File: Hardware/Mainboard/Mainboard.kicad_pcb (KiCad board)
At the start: 4 copper layers, 185.4 x 132.1 mm, 24 parts, among them IC1 TUSB2046BIRHBR, IC2 TUSB2046BIRHBR, IC3 TUSB2046BIRHBR, J1 Conn_02x10_Odd_Even, J10 Conn_02x04_Odd_Even, J11 Conn_02x04_Odd_Even, J12 ARJM11D7-009-AB-EW2, J13 USB4105-GF-A-060, J14 Conn_02x03_Odd_Even, J15 Conn_02x03_Odd_Even, J2 Conn_02x10_Odd_Even, J3 Conn_02x10_Odd_Even, J4 Conn_02x10_Odd_Even, J5 Conn_02x10_Odd_Even, J6 Conn_02x10_Odd_Even, J7 Conn_02x10_Odd_Even, J8 Conn_02x08_Odd_Even, J9 Conn_02x12_Odd_Even, P1 USB-A1HSW6, P2 USB-A1HSW6, SW1 SW_Push_Dual, SW2 SW_Push_Dual, U1 ENC624J600-I/PT, U2 SC0915

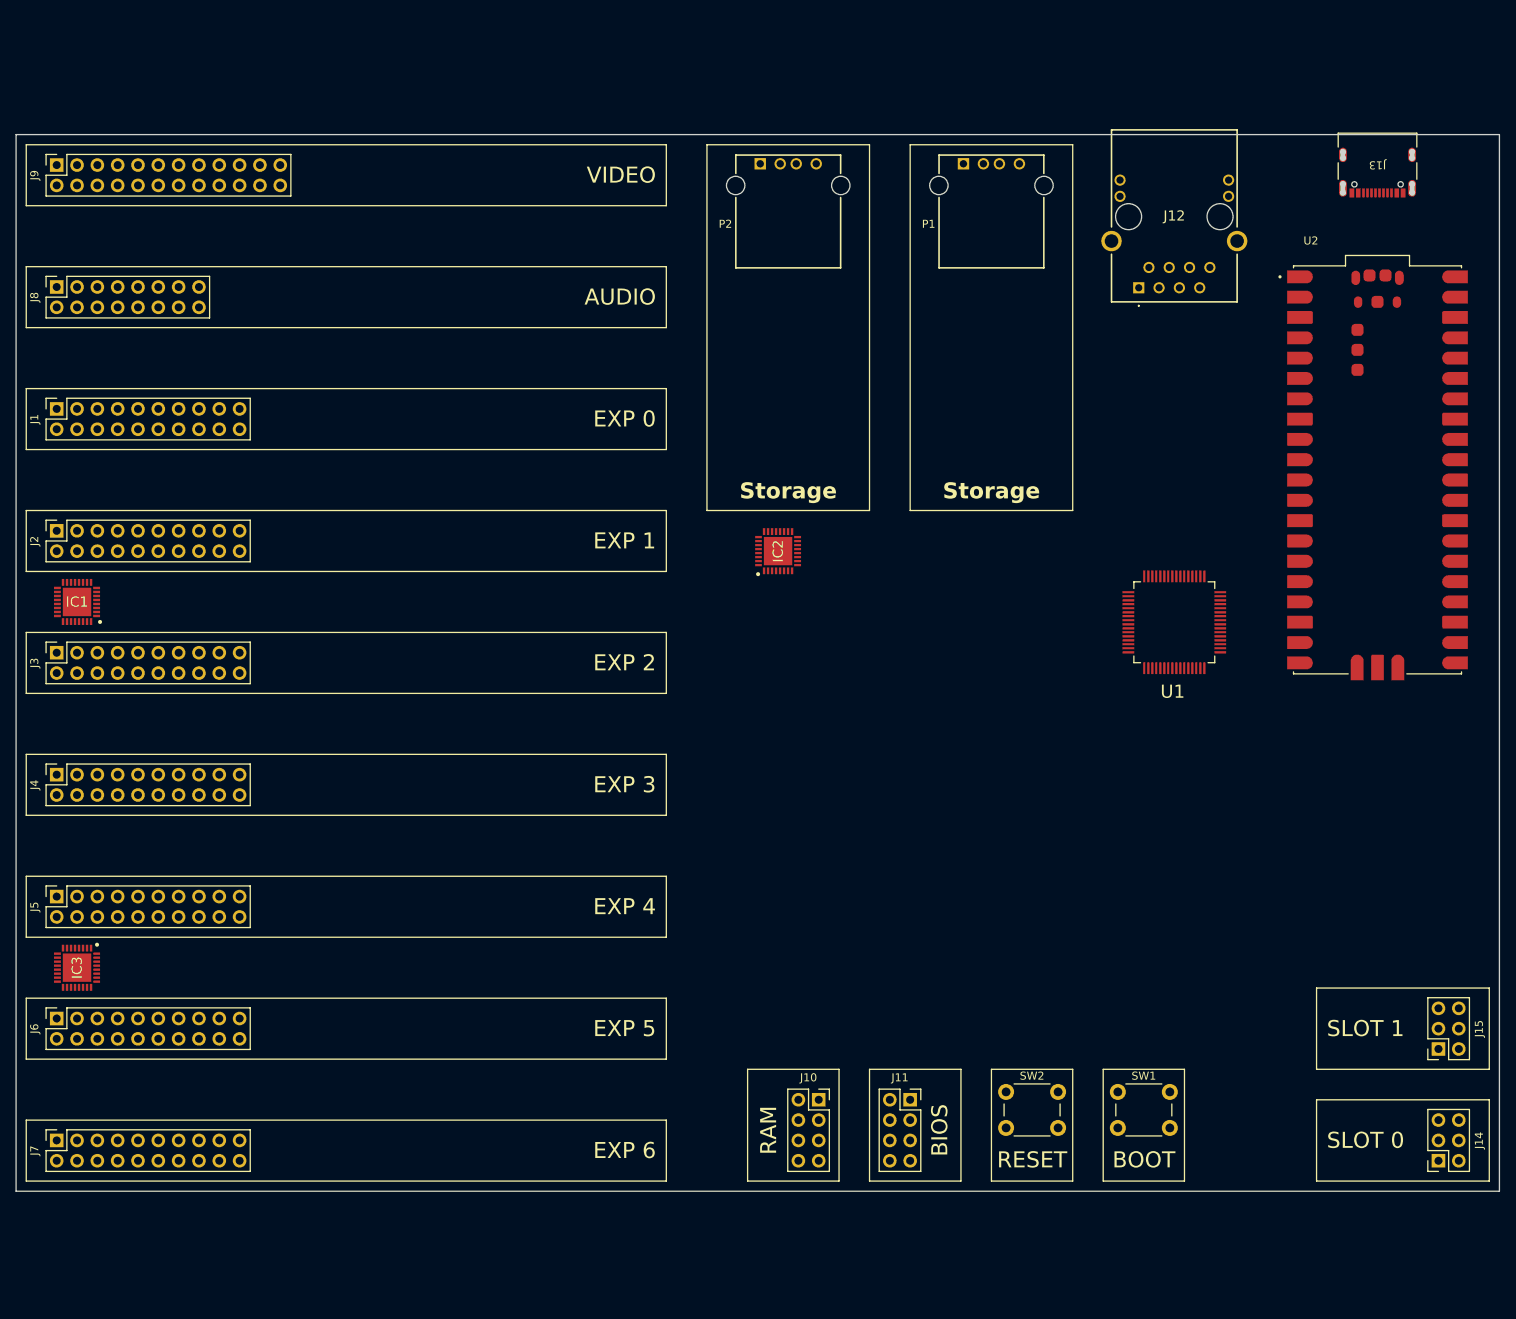
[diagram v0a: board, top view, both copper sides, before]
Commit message: Adds more work on the mainboard schematic
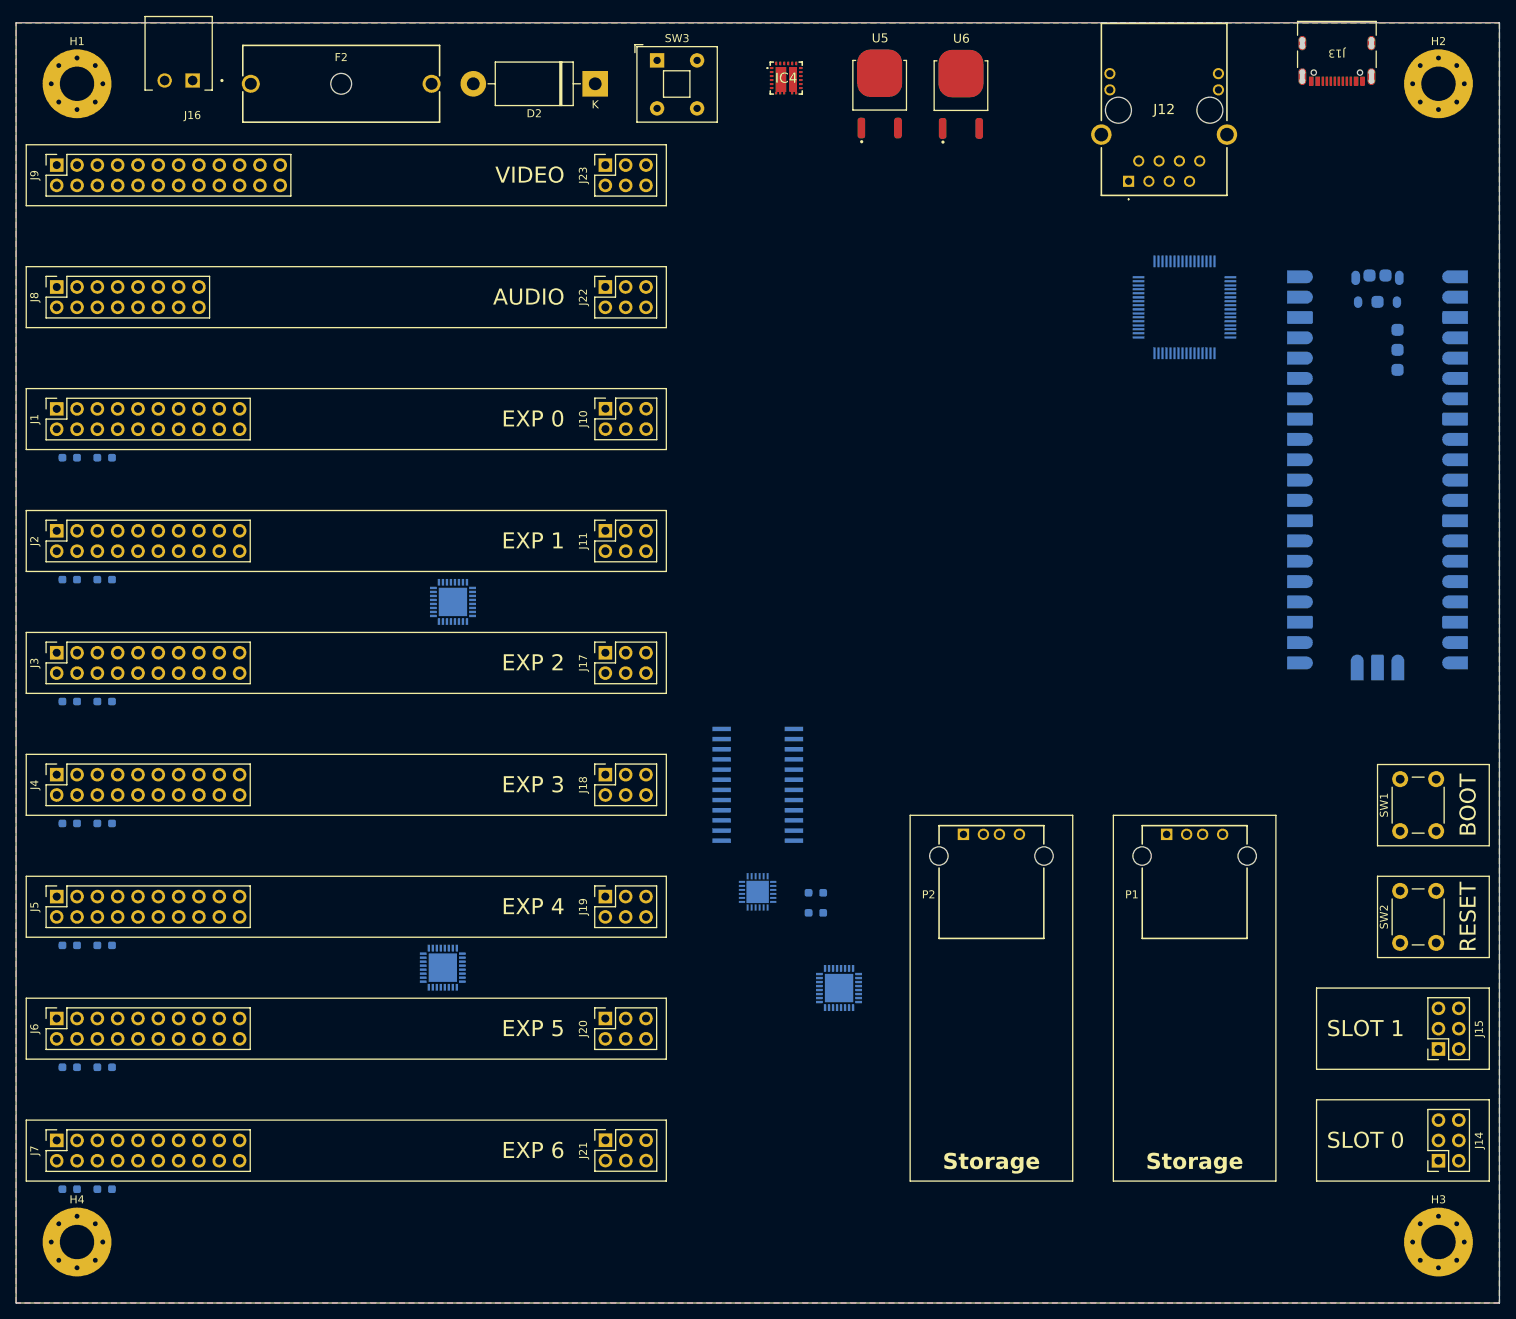
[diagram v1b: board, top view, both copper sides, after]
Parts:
- added D2: 1N5822, Diode_THT:D_DO-201AD_P15.24mm_Horizontal, F.Cu at (115.6, 40.6)
- added F2: 696107003002, compi:696107003002, F.Cu at (83.8, 40.6)
- added H1: MountingHole, MountingHole:MountingHole_4.3mm_M4_Pad_Via, F.Cu at (50.8, 40.6)
- added H2: MountingHole, MountingHole:MountingHole_4.3mm_M4_Pad_Via, F.Cu at (221.0, 40.6)
- added H3: MountingHole, MountingHole:MountingHole_4.3mm_M4_Pad_Via, F.Cu at (221.0, 185.4)
- added H4: MountingHole, MountingHole:MountingHole_4.3mm_M4_Pad_Via, F.Cu at (50.8, 185.4)
- added IC4: AOZ2261NQI-11, compi:aoz2261ngl-11, F.Cu at (139.4, 39.9)
- added J16: 1844210, compi:combicon-1844210, F.Cu at (63.5, 36.8)
- added J17: Conn_02x03_Counter_Clockwise, Connector_PinSocket_2.54mm:PinSocket_2x03_P2.54mm_Vertical, F.Cu at (116.8, 111.8)
- added J18: Conn_02x03_Counter_Clockwise, Connector_PinSocket_2.54mm:PinSocket_2x03_P2.54mm_Vertical, F.Cu at (116.8, 127.0)
- added J19: Conn_02x03_Counter_Clockwise, Connector_PinSocket_2.54mm:PinSocket_2x03_P2.54mm_Vertical, F.Cu at (116.8, 142.2)
- added J20: Conn_02x03_Counter_Clockwise, Connector_PinSocket_2.54mm:PinSocket_2x03_P2.54mm_Vertical, F.Cu at (116.8, 157.5)
- added J21: Conn_02x03_Counter_Clockwise, Connector_PinSocket_2.54mm:PinSocket_2x03_P2.54mm_Vertical, F.Cu at (116.9, 172.7)
- added J22: Conn_02x03_Counter_Clockwise, Connector_PinSocket_2.54mm:PinSocket_2x03_P2.54mm_Vertical, F.Cu at (116.8, 66.0)
- added J23: Conn_02x03_Counter_Clockwise, Connector_PinSocket_2.54mm:PinSocket_2x03_P2.54mm_Vertical, F.Cu at (116.8, 50.8)
- added R1: 10K, Resistor_SMD:R_0603_1608Metric_Pad0.98x0.95mm_HandSolder, B.Cu at (49.9, 87.4)
- added R10: 10K, Resistor_SMD:R_0603_1608Metric_Pad0.98x0.95mm_HandSolder, B.Cu at (54.3, 117.9)
- added R11: 10K, Resistor_SMD:R_0603_1608Metric_Pad0.98x0.95mm_HandSolder, B.Cu at (54.3, 133.1)
- added R12: 10K, Resistor_SMD:R_0603_1608Metric_Pad0.98x0.95mm_HandSolder, B.Cu at (54.3, 148.3)
- added R13: 10K, Resistor_SMD:R_0603_1608Metric_Pad0.98x0.95mm_HandSolder, B.Cu at (54.3, 163.6)
- added R14: 10K, Resistor_SMD:R_0603_1608Metric_Pad0.98x0.95mm_HandSolder, B.Cu at (54.3, 178.8)
- added R15: 10K, Resistor_SMD:R_0603_1608Metric_Pad0.98x0.95mm_HandSolder, B.Cu at (143.2, 141.8)
- added R16: 10K, Resistor_SMD:R_0603_1608Metric_Pad0.98x0.95mm_HandSolder, B.Cu at (143.2, 144.3)
- added R2: 10K, Resistor_SMD:R_0603_1608Metric_Pad0.98x0.95mm_HandSolder, B.Cu at (49.9, 102.6)
- added R3: 10K, Resistor_SMD:R_0603_1608Metric_Pad0.98x0.95mm_HandSolder, B.Cu at (49.9, 117.9)
- added R4: 10K, Resistor_SMD:R_0603_1608Metric_Pad0.98x0.95mm_HandSolder, B.Cu at (49.9, 133.1)
- added R5: 10K, Resistor_SMD:R_0603_1608Metric_Pad0.98x0.95mm_HandSolder, B.Cu at (49.9, 148.3)
- added R6: 10K, Resistor_SMD:R_0603_1608Metric_Pad0.98x0.95mm_HandSolder, B.Cu at (49.9, 163.6)
- added R7: 10K, Resistor_SMD:R_0603_1608Metric_Pad0.98x0.95mm_HandSolder, B.Cu at (49.9, 178.8)
- added R8: 10K, Resistor_SMD:R_0603_1608Metric_Pad0.98x0.95mm_HandSolder, B.Cu at (54.3, 87.4)
- added R9: 10K, Resistor_SMD:R_0603_1608Metric_Pad0.98x0.95mm_HandSolder, B.Cu at (54.3, 102.6)
- added SW3: SW_DPST, Button_Switch_THT:SW_Push_2P1T_Toggle_CK_PVA1xxH1xxxxxxV2, F.Cu at (123.3, 37.7)
- added U3: CD74HC154M96, compi:CD74HC154M96, B.Cu at (135.9, 128.3)
- added U4: TCA9548A, compi:TCA9548ARGERQ1, B.Cu at (135.9, 141.7)
- added U5: AZ1084CD-3.3TRG1, compi:AZ1084CD-3_3TRG1, F.Cu at (151.1, 41.9)
- added U6: AZ1084CD-3.3TRG1, compi:AZ1084CD-3_3TRG1, F.Cu at (161.3, 42.0)
- IC1, IC2, IC3, U1, U2: moved to B.Cu
- J10, J11: value Conn_02x04_Odd_Even -> Conn_02x03_Counter_Clockwise; footprint Connector_PinSocket_2.54mm:PinSocket_2x04_P2.54mm_Vertical -> Connector_PinSocket_2.54mm:PinSocket_2x03_P2.54mm_Vertical
- moved J10 90.4 mm to (116.9, 81.3), turned to 90 degrees
- moved P1 87.6 mm to (190.5, 141.0)
- moved P2 87.6 mm to (165.1, 141.0)
- moved J11 80.7 mm to (116.8, 96.5), turned to 90 degrees
- moved IC2 55.1 mm to (146.1, 153.7), turned to 180 degrees
- moved SW2 52.7 mm to (216.2, 148.0), turned to 90 degrees
- moved SW1 48.0 mm to (216.2, 134.1), turned to 90 degrees
- moved IC1 47.0 mm to (97.8, 105.4), turned to 0 degrees
- moved IC3 45.7 mm to (96.5, 151.1)
- moved U1 39.4 mm to (189.2, 68.6), turned to 0 degrees
- moved J13 14.9 mm to (208.3, 36.8)
- moved J12 13.4 mm to (182.2, 52.8)
- turned U2 to 180 degrees
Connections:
- net /Expansion Subsystem/Expansion Port0/IRQ renamed /Expansion Subsystem/IRQ_{0}
- net /Expansion Subsystem/Expansion Port1/IRQ renamed /Expansion Subsystem/IRQ_{1}
- net /Expansion Subsystem/Expansion Port2/IRQ renamed /Expansion Subsystem/IRQ_{2}
- net /Expansion Subsystem/Expansion Port3/IRQ renamed /Expansion Subsystem/IRQ_{3}
- net /Expansion Subsystem/Expansion Port4/IRQ renamed /Expansion Subsystem/IRQ_{4}
- net /Expansion Subsystem/Expansion Port5/IRQ renamed /Expansion Subsystem/IRQ_{5}
- net /Expansion Subsystem/Expansion Port6/IRQ renamed /Expansion Subsystem/IRQ_{6}
- net /Expansion Subsystem/SPI_{MISO} renamed /SPI_{MISO}
- net /Expansion Subsystem/SPI_{MOSI} renamed /SPI_{MOSI}
- net /Expansion Subsystem/SPI_{SCK} renamed /SPI_{SCK}
- net /USB Subsystem/HOST_{D+} renamed /USB_{D+}
- net /USB Subsystem/HOST_{D-} renamed /USB_{D-}
- J1 pad 11: /Expansion Subsystem/Expansion Port0/SPI_{CS0} -> /Expansion Subsystem/SPI_{CS0}
- J1 pad 12: /Expansion Subsystem/Expansion Port0/SPI_{CS1} -> /Expansion Subsystem/SPI_{CS1}
- J1 pad 4: /Expansion Subsystem/Expansion Port0/I2C_{SCL} -> /Expansion Subsystem/I2C0_{SCL}
- J1 pad 6: /Expansion Subsystem/Expansion Port0/I2C_{SDA} -> /Expansion Subsystem/I2C0_{SDA}
- J10 pad 1: /Memory Subsystem/QMI_{CS0} -> GND
- J10 pad 2: +3V3 -> GND
- J10 pad 3: /Memory Subsystem/QMI_{IO1} -> GND
- J10 pad 4: /Memory Subsystem/QMI_{IO3} -> GND
- J10 pad 5: /Memory Subsystem/QMI_{IO2} -> GND
- J10 pad 6: /Memory Subsystem/QMI_{IO0} -> GND
- J11 pad 1: /Memory Subsystem/QMI_{CS1} -> GND
- J11 pad 2: +3V3 -> GND
- J11 pad 3: /Memory Subsystem/QMI_{IO1} -> GND
- J11 pad 4: /Memory Subsystem/QMI_{IO3} -> GND
- J11 pad 5: /Memory Subsystem/QMI_{IO2} -> GND
- J11 pad 6: /Memory Subsystem/QMI_{IO0} -> GND
- J2 pad 11: /Expansion Subsystem/Expansion Port1/SPI_{CS0} -> /Expansion Subsystem/SPI_{CS2}
- J2 pad 12: /Expansion Subsystem/Expansion Port1/SPI_{CS1} -> /Expansion Subsystem/SPI_{CS3}
- J2 pad 4: /Expansion Subsystem/Expansion Port1/I2C_{SCL} -> /Expansion Subsystem/I2C1_{SCL}
- J2 pad 6: /Expansion Subsystem/Expansion Port1/I2C_{SDA} -> /Expansion Subsystem/I2C1_{SDA}
- J3 pad 11: /Expansion Subsystem/Expansion Port2/SPI_{CS0} -> /Expansion Subsystem/SPI_{CS4}
- J3 pad 12: /Expansion Subsystem/Expansion Port2/SPI_{CS1} -> /Expansion Subsystem/SPI_{CS5}
- J3 pad 4: /Expansion Subsystem/Expansion Port2/I2C_{SCL} -> /Expansion Subsystem/I2C2_{SCL}
- J3 pad 6: /Expansion Subsystem/Expansion Port2/I2C_{SDA} -> /Expansion Subsystem/I2C2_{SDA}
- J4 pad 11: /Expansion Subsystem/Expansion Port3/SPI_{CS0} -> /Expansion Subsystem/SPI_{CS6}
- J4 pad 12: /Expansion Subsystem/Expansion Port3/SPI_{CS1} -> /Expansion Subsystem/SPI_{CS7}
- J4 pad 4: /Expansion Subsystem/Expansion Port3/I2C_{SCL} -> /Expansion Subsystem/I2C3_{SCL}
- J4 pad 6: /Expansion Subsystem/Expansion Port3/I2C_{SDA} -> /Expansion Subsystem/I2C3_{SDA}
- J5 pad 11: /Expansion Subsystem/Expansion Port4/SPI_{CS0} -> /Expansion Subsystem/SPI_{CS8}
- J5 pad 12: /Expansion Subsystem/Expansion Port4/SPI_{CS1} -> /Expansion Subsystem/SPI_{CS9}
- J5 pad 4: /Expansion Subsystem/Expansion Port4/I2C_{SCL} -> /Expansion Subsystem/I2C4_{SCL}
- J5 pad 6: /Expansion Subsystem/Expansion Port4/I2C_{SDA} -> /Expansion Subsystem/I2C4_{SDA}
- J6 pad 11: /Expansion Subsystem/Expansion Port5/SPI_{CS0} -> /Expansion Subsystem/SPI_{CS10}
- J6 pad 12: /Expansion Subsystem/Expansion Port5/SPI_{CS1} -> /Expansion Subsystem/SPI_{CS11}
- J6 pad 4: /Expansion Subsystem/Expansion Port5/I2C_{SCL} -> /Expansion Subsystem/I2C5_{SCL}
- J6 pad 6: /Expansion Subsystem/Expansion Port5/I2C_{SDA} -> /Expansion Subsystem/I2C5_{SDA}
- J7 pad 11: /Expansion Subsystem/Expansion Port6/SPI_{CS0} -> /Expansion Subsystem/SPI_{CS12}
- J7 pad 12: /Expansion Subsystem/Expansion Port6/SPI_{CS1} -> /Expansion Subsystem/SPI_{CS13}
- J7 pad 4: /Expansion Subsystem/Expansion Port6/I2C_{SCL} -> /Expansion Subsystem/I2C6_{SCL}
- J7 pad 6: /Expansion Subsystem/Expansion Port6/I2C_{SDA} -> /Expansion Subsystem/I2C6_{SDA}
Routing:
- added copper zone on In1.Cu, net +3V3
- added copper zone on In2.Cu, net +5V
- added copper zone on B.Cu, net GND
- added copper zone on F.Cu, net GND
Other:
- board size 185.4 x 132.1 mm -> 185.4 x 160 mm
- board text removed: "BIOS"
- board text removed: "RAM"
